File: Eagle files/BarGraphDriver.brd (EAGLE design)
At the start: 100 x 80 mm, 32 parts, among them IC1 74HC595D, IC2 74HC595D

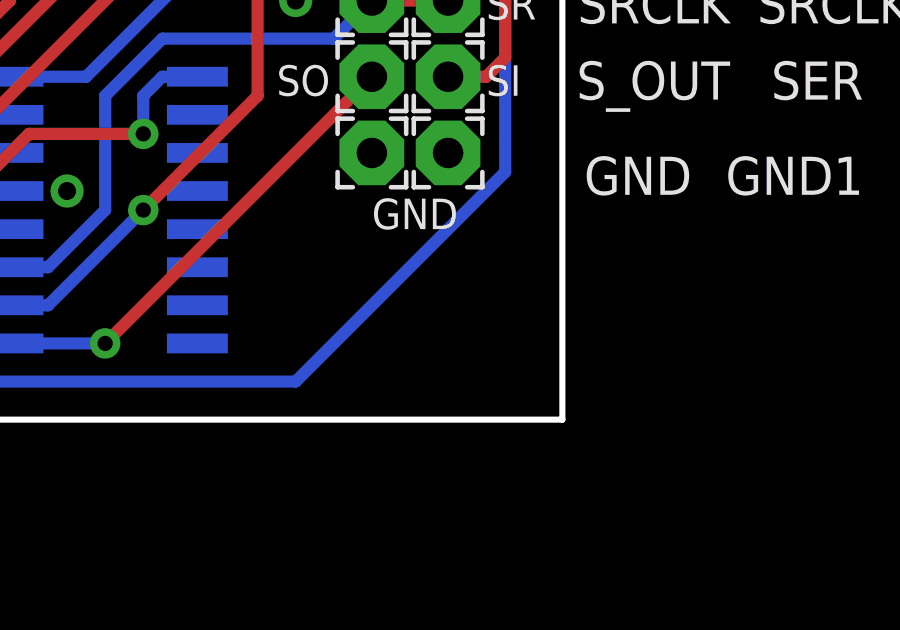
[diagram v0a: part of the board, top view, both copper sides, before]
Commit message: Ready for Fabbing
Silk Screens added and last minute DRC checks done.
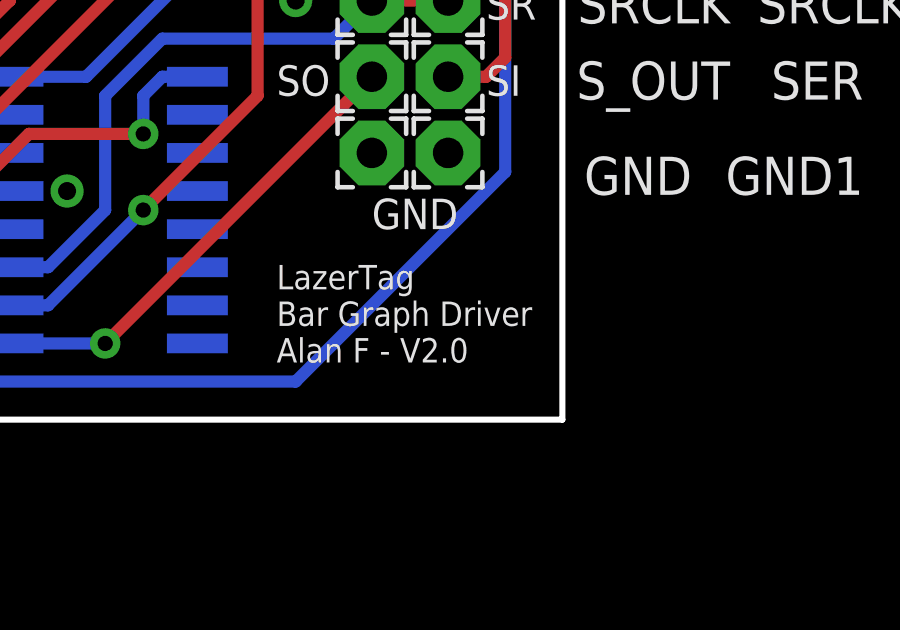
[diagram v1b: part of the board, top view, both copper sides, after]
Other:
- board text added: "LazerTag Bar Graph Driver Alan F - V2.0"
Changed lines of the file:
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@@
 <text x="45.72" y="36.195" size="1.016" layer="21">SR</text>
 <text x="45.72" y="38.735" size="1.016" layer="21">RC</text>
+<text x="38.735" y="24.765" size="0.8128" layer="21">LazerTag
+Bar Graph Driver
+Alan F - V2.0</text>
 </plain>
 <attributes>
@@
 </board>
 </drawing>
+<compatibility>
+<note version="6.3" minversion="6.2.2" severity="warning">
+Since Version 6.2.2 text objects can contain more than one line,
+which will not be processed correctly with this version.
+</note>
+</compatibility>
 </eagle>
